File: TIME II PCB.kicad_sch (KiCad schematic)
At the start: 77 parts, among them J1 USB_C_Receptacle, J2 SD_Card, J4 Conn_01x06, J5 Conn_01x06, J6 Conn_01x06, J7 Conn_01x02_Male, J8 Conn_01x02_Male, Q1 VNP10N07, Q4 VNP10N07, Q5 VNP10N07, SW3 SW_SPDT, U2 ADP2303, U3 LTC4420CMSE-PBF, U7 STM32F103C8Tx, Y1 16 khz

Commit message: new board layout
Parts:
- removed C10: .1uF, Capacitor_SMD:C_0402_1005Metric, symbol Device:C
- removed C11, C9: 2.2uF, Capacitor_SMD:C_0402_1005Metric, symbol Device:C
- removed C12, C14: 47uF, Capacitor_SMD:C_0402_1005Metric, symbol Device:C
- removed C13: 15uF, Capacitor_SMD:C_0402_1005Metric, symbol Device:C
- removed C7: 4.7 uF, Capacitor_SMD:C_0402_1005Metric, symbol Device:C
- removed C8: 10uF, Capacitor_SMD:C_0402_1005Metric, symbol Device:C
- removed D6: D, Diode_SMD:D_0402_1005Metric, symbol Device:D
- removed D7: D_Schottky, Diode_SMD:D_0603_1608Metric_Pad1.05x0.95mm_HandSolder, symbol Device:D_Schottky
- removed L1: 2.2uH, inductor:IND_B1047AS-2R2N=P3, symbol Device:L
- removed MAX2: MAX17610, Package_DFN_QFN:WDFN-12-1EP_3x3mm_P0.45mm_EP1.7x2.5mm, symbol MAX17608:MAX17610
- removed R15: .5, Resistor_SMD:R_0402_1005Metric, symbol Device:R
- removed R16: 15.2k, Resistor_SMD:R_0402_1005Metric, symbol Device:R
- removed R17, R32: 10.2k, Resistor_SMD:R_0402_1005Metric, symbol Device:R
- removed R23: 100k, Resistor_SMD:R_0402_1005Metric, symbol Device:R
- removed R24, R28: 300k, Resistor_SMD:R_0402_1005Metric, symbol Device:R
- removed R25: 154k, Resistor_SMD:R_0402_1005Metric, symbol Device:R
- removed R25.5: 2k, Resistor_SMD:R_0402_1005Metric, symbol Device:R
- removed R26: 45k, Resistor_SMD:R_0402_1005Metric, symbol Device:R
- removed R27, R30: 1M, Resistor_SMD:R_0402_1005Metric, symbol Device:R
- removed R29: 200k, Resistor_SMD:R_0402_1005Metric, symbol Device:R
- removed R31: 31.6k, Resistor_SMD:R_0402_1005Metric, symbol Device:R
- removed RSETI1: 1.8K, Resistor_SMD:R_0402_1005Metric, symbol Device:R
- removed U2: ADP2303, Package_SO:SOIC-8-N7_3.9x4.9mm_P1.27mm, symbol 2022-04-09_08-39-50:ADP2303ARDZ-3.3-R7
- added C16: 15uF, Capacitor_SMD:C_0402_1005Metric, symbol Device:C
- added C17, C20: 2.2uF, Capacitor_SMD:C_0402_1005Metric, symbol Device:C
- added F2: Fuse, Fuse:Fuse_0603_1608Metric, symbol Device:Fuse
- added J8: Conn_01x02_Pin, Connector_JST:JST_XH_B2B-XH-AM_1x02_P2.50mm_Vertical, symbol Connector:Conn_01x02_Pin
- added R10, R12: 1M, Resistor_SMD:R_0402_1005Metric, symbol Device:R
- added R11: 2K, Resistor_SMD:R_0603_1608Metric, symbol Device:R
- added R13: 45K, Resistor_SMD:R_0603_1608Metric, symbol Device:R
- added R13.1: 154K, Resistor_SMD:R_0603_1608Metric, symbol Device:R
- added R19: 86.6K, Resistor_SMD:R_0402_1005Metric, symbol Device:R
- added R8: 0.5, Resistor_SMD:R_0402_1005Metric, symbol Device:R
- added R9: 300K, Resistor_SMD:R_0603_1608Metric, symbol Device:R
- C6: value 0.47 uF -> 10nF
- J1: renamed from J2; footprint sdcard:MEM2075-00-140-01-A_GCT -> GTFP08431BEU:AMPHENOL_GTFP08431BEU; symbol Connector:SD_Card -> sdcardd:GTFP08431BEU; MANUFACTURER (none) -> Amphenol; MAXIMUM_PACKAGE_HEIGHT (none) -> 1.85 mm; PARTREV (none) -> F; SNAPEDA_PN (none) -> GTFP08431BEU; STANDARD (none) -> Manufacturer Recommendations
- R14: value 150K -> 576K
- renumbered C17 to C1, C28 to C10, C29 to C11, C1 to C12, C2 to C13, C15 to C14, C16 to C15, C3 to C18, C5 to C19, C18 to C2, C19 to C3, C25 to C4, C30 to C5, C26 to C8, C27 to C9, H2 to H1, H1 to H2, J1 to J2, J4 to J3, J6 to J4, J8 to J6, Q4 to Q1, Q5 to Q2, Q1 to Q3, R3 to R1, R1 to R15, R12 to R16, R10 to R17, R9 to R18, R6 to R2, R7 to R3, R8 to R4, R11 to R5, R2 to R6, R4 to R7, SW3 to SW1, U7 to U1, U3 to U2, U1 to U3
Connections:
- net 3v3: now also C6.1; no longer U1.24 (VDD), U1.36 (VDD), U1.48 (VDD), U1.9 (VDDA)
- net 5v: no longer C12.1, C13.1, C14.1, C15.1, U2.1 (V1), U2.10 (V2UV), U2.9 (OUT), U3.12 (VM), U4.12 (VM)
- net BAT: now also R14.1, C20.1, F2.2
- net BAT_REAL: now also F2.1, J8.1 (Pin_1)
- net GND: now also J1.G1 (SHIELD_GND), J1.G2 (SHIELD_GND__1), J1.G3 (SHIELD_GND__2), C16.2, C17.2, C20.2, J8.2 (Pin_2), R13.2; no longer J1.12 (SHELL1), J1.13 (SHELL2), J1.3 (VSS), R14.2
- net MISO: now also J1.3 (CMD); no longer J1.2 (CMD)
- net SS: now also J1.2 (CD/DAT3); no longer J1.1 (CD/DAT3)
- net USB_P: now also C12.1, C13.1, C14.1, C15.1, U2.1 (V1), U3.12 (VM), U4.12 (VM), R8.1, R9.1; no longer C6.1
- net at U2.7 (GNDSW): now also R19.2
- net at U2.6 (CMPOUT1): now also R10.2; no longer U2.8 (V2OK)
- net at U2.3 (CMP1): now also R13.1, R13.1.1
- net at U2.4 (ADJ): now also R11.2, R9.2
- net HEAT_POW: now reaches U2.2 (V2TEST)
- net HEAT_POW: now also U2.9 (OUT), C16.1, R10.1, R12.1
- new net: R12.2, U2.8 (V2OK)
- new net: R14.2, R19.1, U2.10 (V2UV)
- new net: C17.1, R8.2
- new net: R11.1, R13.1.2
- new net: U1.36 (VDD), U1.48 (VDD), U1.9 (VDDA)
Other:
- note added: "STM32"
- note removed: "ESP32"
- note removed: "Voltage Regulator 5v -> 3.3v"
- moved on the sheet: C12, C13, C14, C15, C18, C19, C8, R15, R16, R17, R18, U2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

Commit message: major reroute
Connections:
- net MOT_CON2: now also U1.10 (PA0); no longer U1.14 (PA4)
- net MOT_MON_1: now also U1.2 (PC13); no longer U1.40 (PB4)
- net MOT_MON_2: now also U1.13 (PA3); no longer U1.15 (PA5)
- net SERVO_2: now also U1.11 (PA1); no longer U1.16 (PA6)
- net SERVO_2A: now also U1.12 (PA2); no longer U1.13 (PA3)
- net V_MON: now also U1.46 (PB9); no longer U1.18 (PB0)
- net heater_1: now also U1.17 (PA7); no longer U1.11 (PA1)
- net heater_2: now also U1.15 (PA5); no longer U1.45 (PB8)
- net heater_3: now also U1.19 (PB1); no longer U1.29 (PA8)
- net therm_1: now also U1.16 (PA6); no longer U1.12 (PA2)
- net therm_2: now also U1.14 (PA4); no longer U1.10 (PA0)
- net therm_3: now also U1.18 (PB0); no longer U1.19 (PB1)

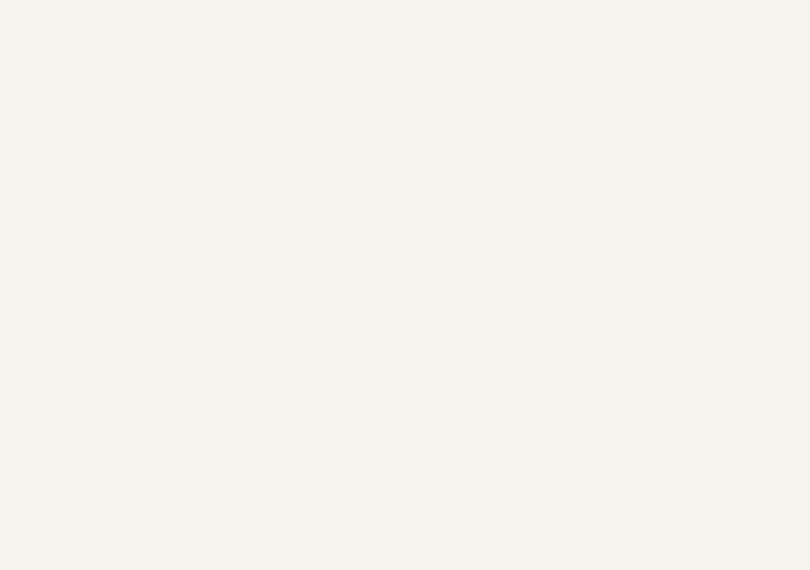
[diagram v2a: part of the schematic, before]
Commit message: ldo added back
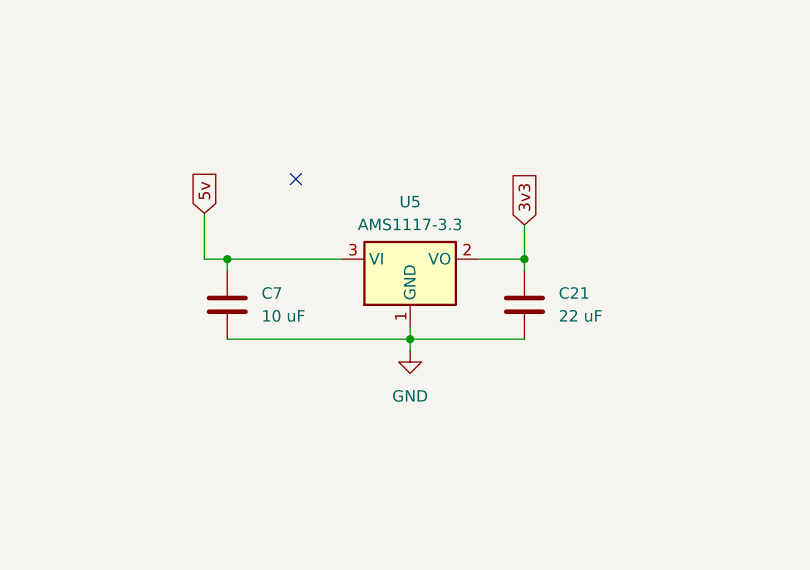
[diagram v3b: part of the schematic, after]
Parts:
- added C21: 22 uF, Capacitor_SMD:C_0402_1005Metric, symbol Device:C
- added C7: 10 uF, Capacitor_SMD:C_0402_1005Metric, symbol Device:C
- added U5: AMS1117-3.3, Package_TO_SOT_SMD:SOT-223-3_TabPin2, symbol Regulator_Linear:AMS1117-3.3
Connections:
- net 3v3: now also C21.1, U5.2 (VO)
- net 5v: now also C7.1, U5.3 (VI)
- net GND: now also C21.2, C7.2, U5.1 (GND)
- no-connect marks 1 -> 2

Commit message: Update README
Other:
- note added: "5V-3V3 LDO"
- note added: "DRV8837 Motor Controllers"
- note added: "INDICATOR LEDS + Other Small Subcircuits"
- note removed: "INDICATOR LEDS"
- moved on the sheet: C1, C10, C11, C12, C13, C14, C15, C16, C17, C18, C19, C2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

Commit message: week of 01/10/24
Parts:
- J1: footprint GTFP08431BEU:AMPHENOL_GTFP08431BEU -> 114_00841_68:AMPHENOL_1140084168
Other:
- moved on the sheet: C12, C13, C14, C15, C16, C17, C18, C19, C20, C21, C7, D1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
